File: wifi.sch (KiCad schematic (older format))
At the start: 8 parts

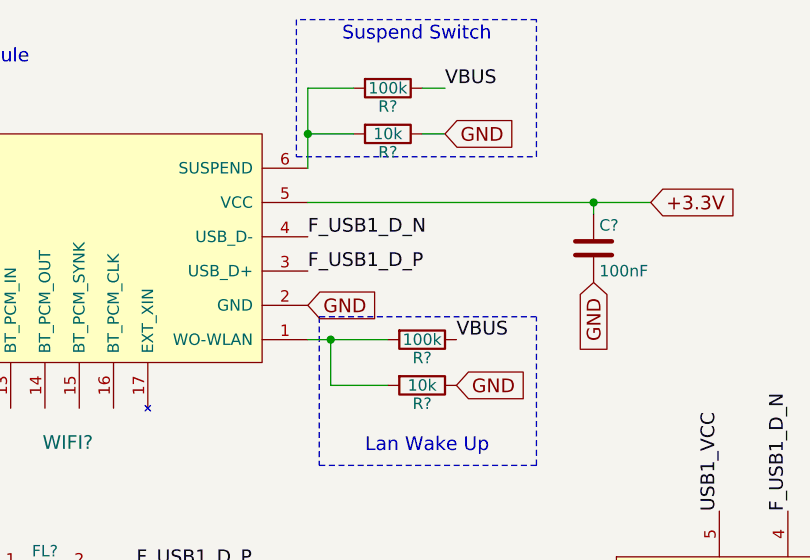
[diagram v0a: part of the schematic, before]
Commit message: this version contains the datasheets and the footprints of the parts
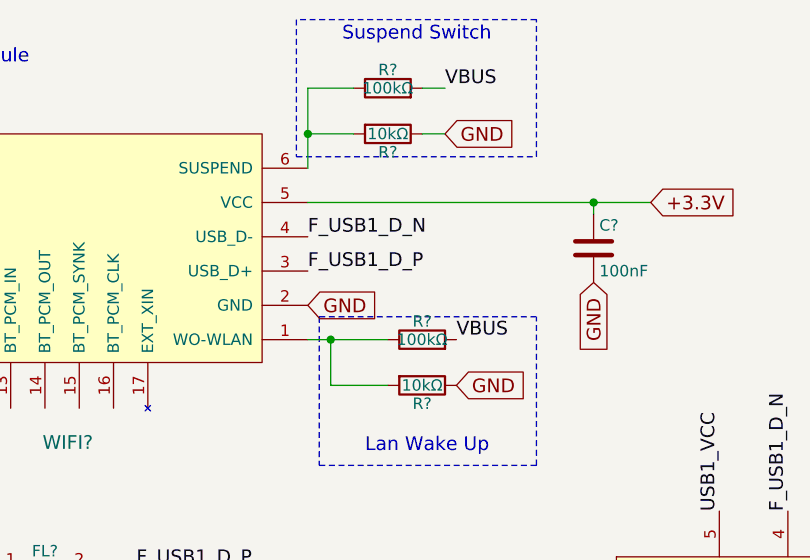
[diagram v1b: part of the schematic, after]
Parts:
- removed C?: 100nF, symbol C
- removed R?: 10k, symbol R
- removed R? (x2): 100k, symbol R
- added C?: 100nF, Capacitors_SMD:C_0603_HandSoldering, symbol C
- added R?: 10kΩ, Resistors_SMD:R_0603_HandSoldering, symbol R
- added R? (x2): 100kΩ, Resistors_SMD:R_0603_HandSoldering, symbol R
- FL?: footprint (none) -> water:744233121
- R?: value 10k -> 10kΩ; footprint (none) -> Resistors_SMD:R_0603_HandSoldering
- TVS?: footprint (none) -> Housings_SOT-23_SOT-143_TSOT-6:SOT-23-5
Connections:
- net +3.3V: now also C?.1
- net GND: now also C?.2, R?.1
- net VBUS: now also R?.2, R?.2
- net at WIFI?.1 (WO-WLAN): now also R?.1, R?.2
- net at R?.2, WIFI?.6 (SUSPEND): now also R?.1
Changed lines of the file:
@@
 Text GLabel 3300 1850 2    60   Input ~ 0
 GND
-$Comp
-L R R?
-U 1 1 599FE3F1
-P 3800 2200
-F 0 "R?" V 3880 2200 50  0000 C CNN
-F 1 "10k" V 3800 2200 50  0000 C CNN
-F 2 "" V 3730 2200 50  0001 C CNN
-F 3 "" H 3800 2200 50  0001 C CNN
-	1    3800 2200
-	0    1    1    0
-$EndComp
-$Comp
-L R R?
-U 1 1 599FE3F8
-P 3800 2000
-F 0 "R?" V 3880 2000 50  0000 C CNN
-F 1 "100k" V 3800 2000 50  0000 C CNN
-F 2 "" V 3730 2000 50  0001 C CNN
-F 3 "" H 3800 2000 50  0001 C CNN
-	1    3800 2000
-	0    1    1    0
-$EndComp
 Text GLabel 3950 2200 2    60   Input ~ 0
 GND
@@
 $Comp
 L R R?
-U 1 1 599FE408
-P 3650 900
-F 0 "R?" V 3730 900 50  0000 C CNN
-F 1 "100k" V 3650 900 50  0000 C CNN
-F 2 "" V 3580 900 50  0001 C CNN
-F 3 "" H 3650 900 50  0001 C CNN
-	1    3650 900
-	0    1    1    0
-$EndComp
-$Comp
-L R R?
 U 1 1 599FE410
 P 3650 1100
 F 0 "R?" V 3730 1100 50  0000 C CNN
-F 1 "10k" V 3650 1100 50  0000 C CNN
-F 2 "" V 3580 1100 50  0001 C CNN
-F 3 "" H 3650 1100 50  0001 C CNN
+F 1 "10kΩ" V 3650 1100 50  0000 C CNN
+F 2 "Resistors_SMD:R_0603_HandSoldering" V 3580 1100 50  0001 C CNN
+F 3 "http://hu.farnell.com/multicomp/mcwr06x1002ftl/res-thick-film-10k-1-0-1w-0603/dp/2447230" H 3650 1100 50  0001 C CNN
 	1    3650 1100
 	0    1    1    0
@@
 F 0 "FL?" H 2150 3275 50  0000 C CNN
 F 1 "EMI_Filter_CommonMode" H 2150 2925 50  0000 C CNN
-F 2 "" V 2150 3140 50  0000 C CNN
+F 2 "water:744233121" V 2150 3140 50  0001 C CNN
 F 3 "http://hu.farnell.com/wurth-elektronik/744233121/line-filter-lvds-0805-120ohm-0/dp/1848957" V 2150 3140 50  0001 C CNN
 	1    2150 3100
@@
 F 0 "TVS?" V 5650 3150 60  0000 C CNN
 F 1 "824011" V 4550 3150 60  0000 C CNN
-F 2 "" H 5950 3200 60  0001 C CNN
-F 3 "" H 5950 3200 60  0001 C CNN
+F 2 "Housings_SOT-23_SOT-143_TSOT-6:SOT-23-5" H 5950 3200 60  0001 C CNN
+F 3 "http://hu.farnell.com/wurth-elektronik/824011/diode-array-tvs/dp/1748616" H 5950 3200 60  0001 C CNN
 	1    5950 3200
 	1    0    0    -1
@@
 Text GLabel 4550 1750 3    60   Input ~ 0
 GND
-$Comp
-L C C?
-U 1 1 59A29FEC
-P 4550 1600
-F 0 "C?" H 4575 1700 50  0000 L CNN
-F 1 "100nF" H 4575 1500 50  0000 L CNN
-F 2 "" H 4588 1450 50  0001 C CNN
-F 3 "" H 4550 1600 50  0001 C CNN
-	1    4550 1600
-	1    0    0    -1
-$EndComp
 Wire Wire Line
 	3300 1250 3300 900
@@
 Wire Notes Line
 	3250 600  3250 1200
+$Comp
+L R R?
+U 1 1 59A84285
+P 3800 2000
+F 0 "R?" V 3880 2000 50  0000 C CNN
+F 1 "100kΩ" V 3800 2000 50  0000 C CNN
+F 2 "Resistors_SMD:R_0603_HandSoldering" V 3730 2000 30  0001 C CNN
+F 3 "hu.farnell.com/multicomp/mcmr06x104-jtl/res-ceramic-100k-5-0-1w-0603/dp/2073357" H 3800 2000 30  0001 C CNN
+	1    3800 2000
+	0    -1   -1   0
+$EndComp
+$Comp
+L R R?
+U 1 1 59A8431F
+P 3650 900
+F 0 "R?" V 3730 900 50  0000 C CNN
+F 1 "100kΩ" V 3650 900 50  0000 C CNN
+F 2 "Resistors_SMD:R_0603_HandSoldering" V 3580 900 30  0001 C CNN
+F 3 "hu.farnell.com/multicomp/mcmr06x104-jtl/res-ceramic-100k-5-0-1w-0603/dp/2073357" H 3650 900 30  0001 C CNN
+	1    3650 900
+	0    -1   -1   0
+$EndComp
+$Comp
+L C C?
+U 1 1 59A67E6E
+P 4550 1600
+F 0 "C?" H 4575 1700 50  0000 L CNN
+F 1 "100nF" H 4575 1500 50  0000 L CNN
+F 2 "Capacitors_SMD:C_0603_HandSoldering" H 4588 1450 30  0001 C CNN
+F 3 "hu.farnell.com/avx/06035c104kat2a/cap-mlcc-x7r-100nf-50v-0603/dp/1301804" H 4550 1600 60  0001 C CNN
+	1    4550 1600
+	1    0    0    -1
+$EndComp
+$Comp
+L R R?
+U 1 1 59A6BB57
+P 3800 2200
+F 0 "R?" V 3880 2200 50  0000 C CNN
+F 1 "10kΩ" V 3800 2200 50  0000 C CNN
+F 2 "Resistors_SMD:R_0603_HandSoldering" V 3730 2200 50  0001 C CNN
+F 3 "http://hu.farnell.com/multicomp/mcwr06x1002ftl/res-thick-film-10k-1-0-1w-0603/dp/2447230" H 3800 2200 50  0001 C CNN
+	1    3800 2200
+	0    1    1    0
+$EndComp
 $EndSCHEMATC

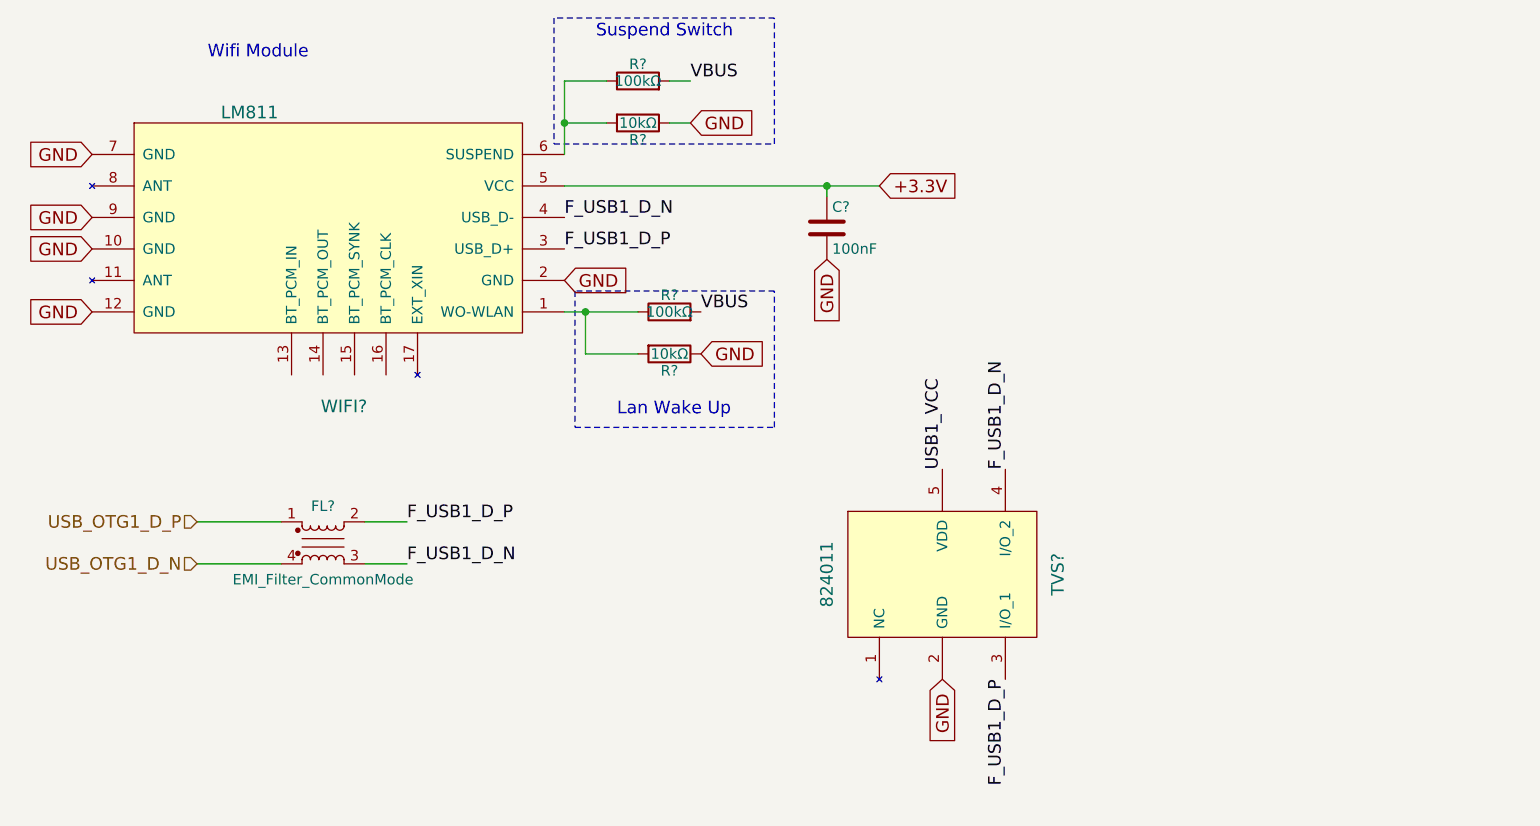
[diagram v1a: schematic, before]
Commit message: some issues fixed by the bugfixer; formal verification needed
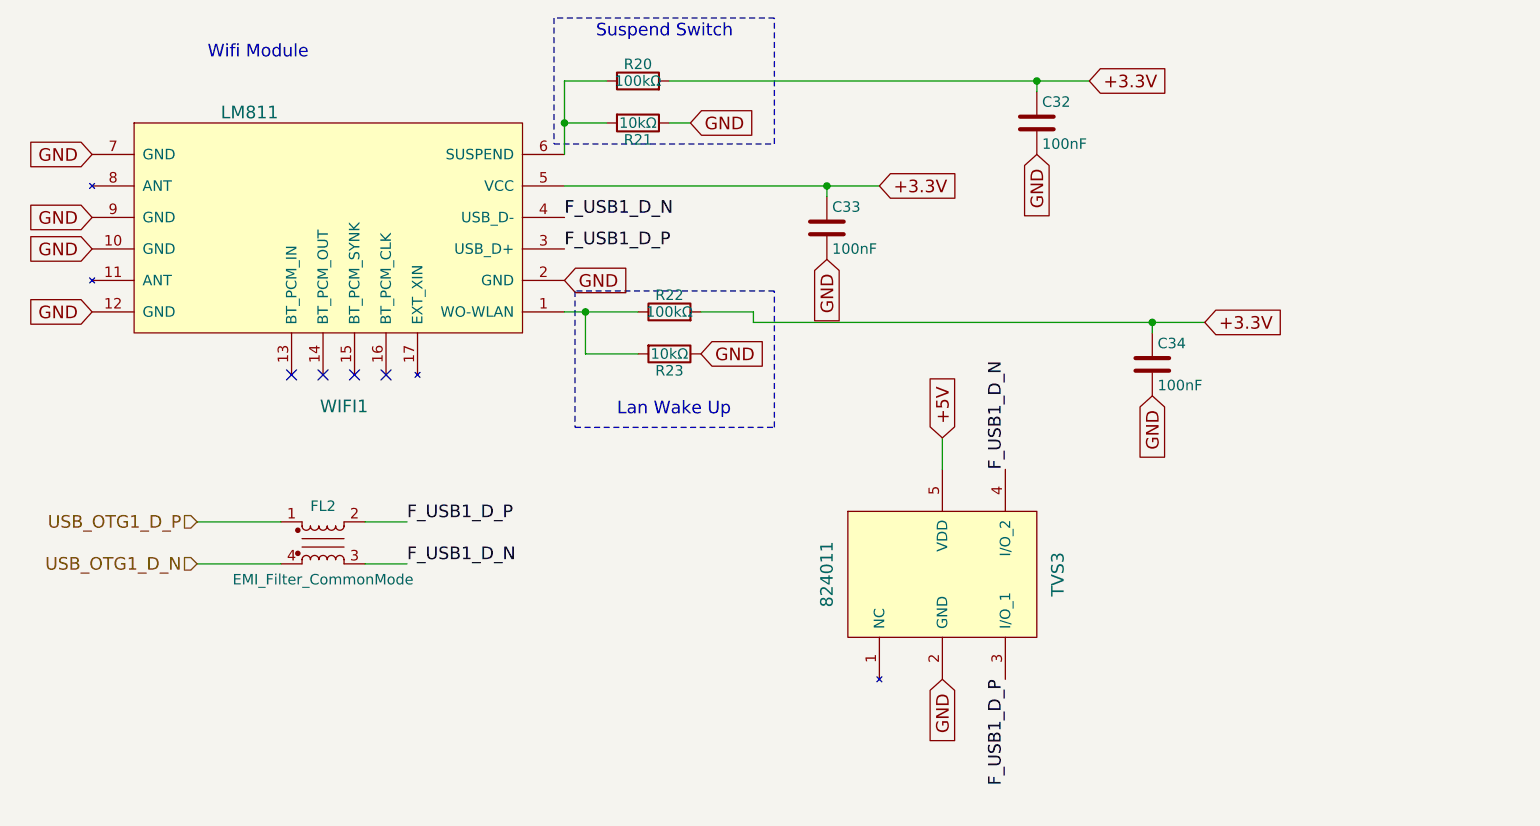
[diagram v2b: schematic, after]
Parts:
- added C32, C34: 100nF, Capacitors_SMD:C_0603_HandSoldering, symbol C
- gave numbers to parts that had none: 8
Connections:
- net VBUS is gone; now on net +3.3V: R20.2, R22.2
- net +3.3V: now also C32.1, C34.1
- net GND: now also C32.2, C34.2
- net USB1_VCC renamed +5V
- no-connect marks 0 -> 4
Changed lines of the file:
@@
 $EndDescr
 $Comp
-L LM811 WIFI?
+L LM811 WIFI1
 U 1 1 599FE3E1
 P 200 1050
-F 0 "WIFI?" H 2250 -350 60  0000 C CNN
+F 0 "WIFI1" H 2250 -350 60  0000 C CNN
 F 1 "LM811" H 1800 1050 60  0000 C CNN
 F 2 "water:LM811" H 200 1050 60  0001 C CNN
@@
 Suspend Switch
 $Comp
-L R R?
+L R R21
 U 1 1 599FE410
 P 3650 1100
-F 0 "R?" V 3730 1100 50  0000 C CNN
+F 0 "R21" V 3730 1100 50  0000 C CNN
 F 1 "10kΩ" V 3650 1100 50  0000 C CNN
 F 2 "Resistors_SMD:R_0603_HandSoldering" V 3580 1100 50  0001 C CNN
@@
 Lan Wake Up
 $Comp
-L EMI_Filter_CommonMode FL?
+L EMI_Filter_CommonMode FL2
 U 1 1 59A23483
 P 2150 3100
-F 0 "FL?" H 2150 3275 50  0000 C CNN
+F 0 "FL2" H 2150 3275 50  0000 C CNN
 F 1 "EMI_Filter_CommonMode" H 2150 2925 50  0000 C CNN
 F 2 "water:744233121" V 2150 3140 50  0001 C CNN
@@
 F_USB1_D_N
 $Comp
-L 824011 TVS?
+L 824011 TVS3
 U 1 1 59A26FAC
 P 5950 3200
-F 0 "TVS?" V 5650 3150 60  0000 C CNN
+F 0 "TVS3" V 5650 3150 60  0000 C CNN
 F 1 "824011" V 4550 3150 60  0000 C CNN
 F 2 "Housings_SOT-23_SOT-143_TSOT-6:SOT-23-5" H 5950 3200 60  0001 C CNN
@@
 Text Label 5400 2750 1    60   ~ 0
 F_USB1_D_N
-Text Label 5100 2750 1    60   ~ 0
-USB1_VCC
-Text Label 3900 900  0    60   ~ 0
-VBUS
-Text Label 3950 2000 0    60   ~ 0
-VBUS
 Text GLabel 4800 1400 2    60   Input ~ 0
 +3.3V
@@
 	3800 1100 3900 1100
 Wire Wire Line
-	3800 900  3900 900
+	3800 900  5800 900
 Wire Wire Line
 	1550 3000 1950 3000
@@
 	3250 600  3250 1200
 $Comp
-L R R?
+L R R22
 U 1 1 59A84285
 P 3800 2000
-F 0 "R?" V 3880 2000 50  0000 C CNN
+F 0 "R22" V 3880 2000 50  0000 C CNN
 F 1 "100kΩ" V 3800 2000 50  0000 C CNN
 F 2 "Resistors_SMD:R_0603_HandSoldering" V 3730 2000 30  0001 C CNN
@@
 $EndComp
 $Comp
-L R R?
+L R R20
 U 1 1 59A8431F
 P 3650 900
-F 0 "R?" V 3730 900 50  0000 C CNN
+F 0 "R20" V 3730 900 50  0000 C CNN
 F 1 "100kΩ" V 3650 900 50  0000 C CNN
 F 2 "Resistors_SMD:R_0603_HandSoldering" V 3580 900 30  0001 C CNN
@@
 $EndComp
 $Comp
-L C C?
+L C C33
 U 1 1 59A67E6E
 P 4550 1600
-F 0 "C?" H 4575 1700 50  0000 L CNN
+F 0 "C33" H 4575 1700 50  0000 L CNN
 F 1 "100nF" H 4575 1500 50  0000 L CNN
 F 2 "Capacitors_SMD:C_0603_HandSoldering" H 4588 1450 30  0001 C CNN
@@
 $EndComp
 $Comp
-L R R?
+L R R23
 U 1 1 59A6BB57
 P 3800 2200
-F 0 "R?" V 3880 2200 50  0000 C CNN
+F 0 "R23" V 3880 2200 50  0000 C CNN
 F 1 "10kΩ" V 3800 2200 50  0000 C CNN
 F 2 "Resistors_SMD:R_0603_HandSoldering" V 3730 2200 50  0001 C CNN
@@
 	0    1    1    0
 $EndComp
+Text GLabel 5800 900  2    60   Input ~ 0
++3.3V
+Text GLabel 5550 1250 3    60   Input ~ 0
+GND
+Wire Wire Line
+	5550 950  5550 900
+Connection ~ 5550 900
+$Comp
+L C C32
+U 1 1 59AA68FC
+P 5550 1100
+F 0 "C32" H 5575 1200 50  0000 L CNN
+F 1 "100nF" H 5575 1000 50  0000 L CNN
+F 2 "Capacitors_SMD:C_0603_HandSoldering" H 5588 950 30  0001 C CNN
+F 3 "hu.farnell.com/avx/06035c104kat2a/cap-mlcc-x7r-100nf-50v-0603/dp/1301804" H 5550 1100 60  0001 C CNN
+	1    5550 1100
+	1    0    0    -1
+$EndComp
+Wire Wire Line
+	4200 2050 6350 2050
+Text GLabel 6350 2050 2    60   Input ~ 0
++3.3V
+Text GLabel 6100 2400 3    60   Input ~ 0
+GND
+Wire Wire Line
+	6100 2100 6100 2050
+Connection ~ 6100 2050
+$Comp
+L C C34
+U 1 1 59AA69A3
+P 6100 2250
+F 0 "C34" H 6125 2350 50  0000 L CNN
+F 1 "100nF" H 6125 2150 50  0000 L CNN
+F 2 "Capacitors_SMD:C_0603_HandSoldering" H 6138 2100 30  0001 C CNN
+F 3 "hu.farnell.com/avx/06035c104kat2a/cap-mlcc-x7r-100nf-50v-0603/dp/1301804" H 6100 2250 60  0001 C CNN
+	1    6100 2250
+	1    0    0    -1
+$EndComp
+Wire Wire Line
+	4200 2050 4200 2000
+Wire Wire Line
+	4200 2000 3950 2000
+Text GLabel 5100 2600 1    60   Input ~ 0
++5V
+Wire Wire Line
+	5100 2600 5100 2750
+NoConn ~ 2000 2300
+NoConn ~ 2150 2300
+NoConn ~ 2300 2300
+NoConn ~ 2450 2300
 $EndSCHEMATC

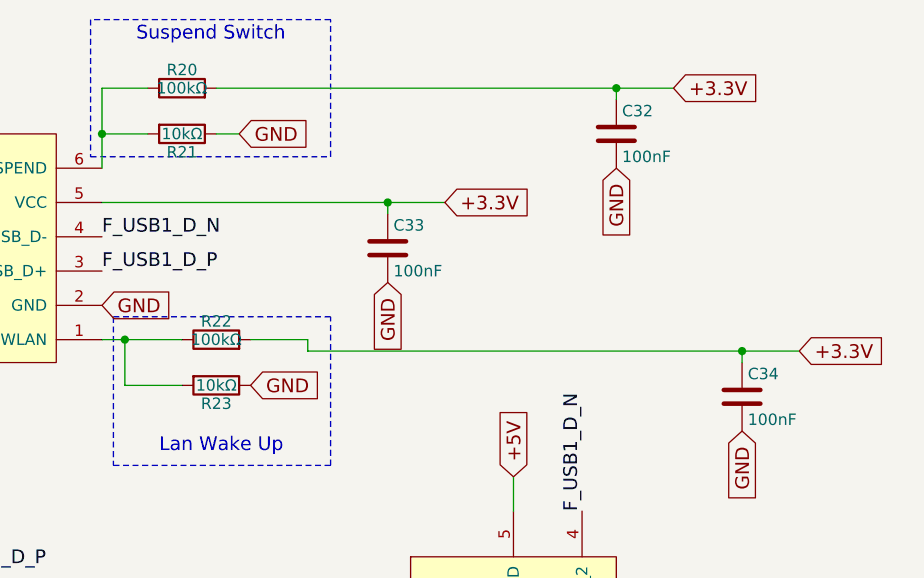
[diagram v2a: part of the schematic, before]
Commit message: part numbers generated;
pcb generation started
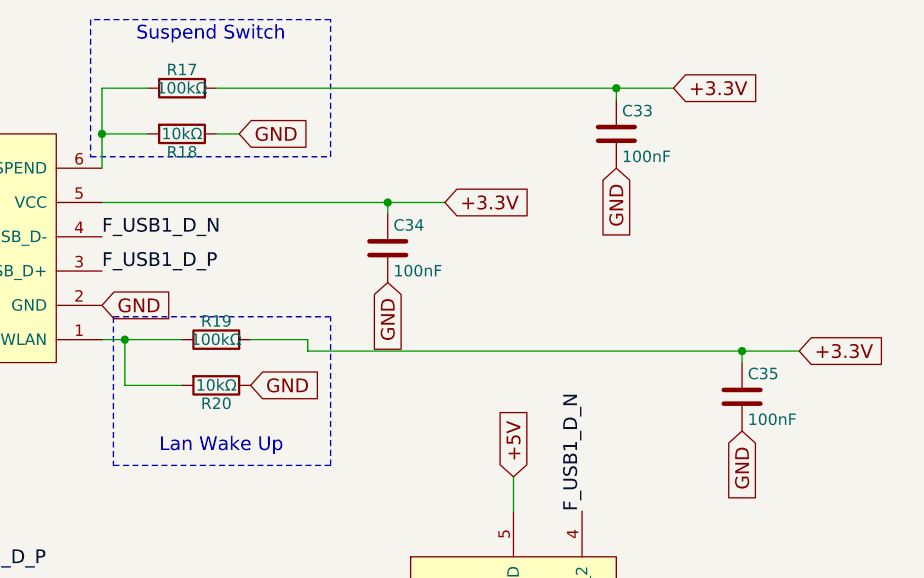
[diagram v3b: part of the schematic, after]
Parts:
- renumbered C32 to C33, C33 to C34, C34 to C35, R20 to R17, R21 to R18, R22 to R19, R23 to R20
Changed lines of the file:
@@
 Suspend Switch
 $Comp
-L R R21
+L R R18
 U 1 1 599FE410
 P 3650 1100
-F 0 "R21" V 3730 1100 50  0000 C CNN
+F 0 "R18" V 3730 1100 50  0000 C CNN
 F 1 "10kΩ" V 3650 1100 50  0000 C CNN
 F 2 "Resistors_SMD:R_0603_HandSoldering" V 3580 1100 50  0001 C CNN
@@
 	3250 600  3250 1200
 $Comp
-L R R22
+L R R19
 U 1 1 59A84285
 P 3800 2000
-F 0 "R22" V 3880 2000 50  0000 C CNN
+F 0 "R19" V 3880 2000 50  0000 C CNN
 F 1 "100kΩ" V 3800 2000 50  0000 C CNN
 F 2 "Resistors_SMD:R_0603_HandSoldering" V 3730 2000 30  0001 C CNN
@@
 $EndComp
 $Comp
-L R R20
+L R R17
 U 1 1 59A8431F
 P 3650 900
-F 0 "R20" V 3730 900 50  0000 C CNN
+F 0 "R17" V 3730 900 50  0000 C CNN
 F 1 "100kΩ" V 3650 900 50  0000 C CNN
 F 2 "Resistors_SMD:R_0603_HandSoldering" V 3580 900 30  0001 C CNN
@@
 $EndComp
 $Comp
-L C C33
+L C C34
 U 1 1 59A67E6E
 P 4550 1600
-F 0 "C33" H 4575 1700 50  0000 L CNN
+F 0 "C34" H 4575 1700 50  0000 L CNN
 F 1 "100nF" H 4575 1500 50  0000 L CNN
 F 2 "Capacitors_SMD:C_0603_HandSoldering" H 4588 1450 30  0001 C CNN
@@
 $EndComp
 $Comp
-L R R23
+L R R20
 U 1 1 59A6BB57
 P 3800 2200
-F 0 "R23" V 3880 2200 50  0000 C CNN
+F 0 "R20" V 3880 2200 50  0000 C CNN
 F 1 "10kΩ" V 3800 2200 50  0000 C CNN
 F 2 "Resistors_SMD:R_0603_HandSoldering" V 3730 2200 50  0001 C CNN
@@
 Connection ~ 5550 900
 $Comp
-L C C32
+L C C33
 U 1 1 59AA68FC
 P 5550 1100
-F 0 "C32" H 5575 1200 50  0000 L CNN
+F 0 "C33" H 5575 1200 50  0000 L CNN
 F 1 "100nF" H 5575 1000 50  0000 L CNN
 F 2 "Capacitors_SMD:C_0603_HandSoldering" H 5588 950 30  0001 C CNN
@@
 Connection ~ 6100 2050
 $Comp
-L C C34
+L C C35
 U 1 1 59AA69A3
 P 6100 2250
-F 0 "C34" H 6125 2350 50  0000 L CNN
+F 0 "C35" H 6125 2350 50  0000 L CNN
 F 1 "100nF" H 6125 2150 50  0000 L CNN
 F 2 "Capacitors_SMD:C_0603_HandSoldering" H 6138 2100 30  0001 C CNN
